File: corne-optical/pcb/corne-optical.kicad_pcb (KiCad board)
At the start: 2 copper layers, 145.7 x 94.9 mm, 77 parts, among them J1 MJ-4PP-9, J2 OLED, J3 LED, J4 Conn_01x02, J5 Conn_01x02, P1 i2c-pin, P2 i2c-pin, SW1 SW_PUSH, SW10 SW_PUSH, SW11 SW_PUSH, SW12 SW_PUSH, SW13 SW_PUSH, SW14 SW_PUSH, SW15 SW_PUSH, SW16 SW_PUSH, SW17 SW_PUSH, SW18 SW_PUSH, SW19 SW_PUSH, SW2 SW_PUSH, SW20 SW_PUSH, SW21 SW_PUSH, SW3 SW_PUSH, SW4 SW_PUSH, SW5 SW_PUSH, SW6 SW_PUSH, SW7 SW_PUSH, SW8 SW_PUSH, SW9 SW_PUSH, U1 ProMicro

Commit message: Trying to workout phantom copper
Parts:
- removed ? (x7): , kbd:LEGO_HOLE
- removed D1, D10, D11, D12, D13, D14, D15, D16, D17, D18, D19, D2, D20, D21, D3, D4, D5, D6, D7, D8, D9: D, kbd:D3_SMD
- removed G*** (x2): LOGO, kbd:corne
- removed L22, L23, L24, L25, L26, L27: SK6812MINI, kbd:SK6812MINI_underglow_rev
- added Q1: Q_NMOS_GSD, Package_TO_SOT_SMD:SOT-23, F.Cu at (75.7, 106.0)
- added Q2: Q_NMOS_GSD, Package_TO_SOT_SMD:SOT-23, F.Cu at (96.0, 106.0)
- added Q3: Q_NMOS_GSD, Package_TO_SOT_SMD:SOT-23, F.Cu at (113.7, 100.8)
- added Q4: Q_NMOS_GSD, Package_TO_SOT_SMD:SOT-23, F.Cu at (132.8, 98.5)
- added Q5: Q_NMOS_GSD, Package_TO_SOT_SMD:SOT-23, F.Cu at (153.5, 100.9)
- added Q6: Q_NMOS_GSD, Package_TO_SOT_SMD:SOT-23, F.Cu at (169.2, 103.2)
- added R10: 70R, Resistor_SMD:R_0603_1608Metric, F.Cu at (61.8, 80.8)
- added R11: 70R, Resistor_SMD:R_0603_1608Metric, F.Cu at (81.0, 80.3)
- added R3: 70R, Resistor_SMD:R_0603_1608Metric, F.Cu at (100.0, 76.3)
- added R4: 70R, Resistor_SMD:R_0603_1608Metric, F.Cu at (118.7, 73.9)
- added R5: 70R, Resistor_SMD:R_0603_1608Metric, F.Cu at (138.2, 76.2)
- added R6: 70R, Resistor_SMD:R_0603_1608Metric, F.Cu at (157.0, 78.6)
- added R7: 190R, Resistor_SMD:R_0603_1608Metric, F.Cu at (145.0, 122.5)
- added R8: 190R, Resistor_SMD:R_0603_1608Metric, F.Cu at (167.6, 130.1)
- added R9: 190R, Resistor_SMD:R_0603_1608Metric, F.Cu at (173.9, 128.3)
- J2: value OLED -> Conn_01x04
- J3: value LED -> Conn_01x03
- JP1: value (none) -> SolderJumper_2_Bridged
- JP2, JP3, JP4, JP5, JP6, JP7, JP8, JP9: value (none) -> SolderJumper_2_Open
- P1, P2: value i2c-pin -> Conn_01x01
- RSW1: value SW_PUSH -> SW_Push
- SW1, SW10, SW11, SW12, SW13, SW14, SW15, SW16, SW17, SW18, SW19, SW2, SW20, SW3, SW4, SW5, SW6, SW7, SW8, SW9: value SW_PUSH -> Keychron_LP_Optical; footprint kbd:Choc_Hotswap -> optical:Keychron_LP_Optical
- SW21: value SW_PUSH -> Keychron_LP_Optical; footprint kbd:Choc_Hotswap_1.5u -> optical:Keychron_LP_Optical_1.5u
- turned SW1 to 0 degrees
- turned SW10 to 0 degrees
- turned SW11 to 0 degrees
- turned SW12 to 0 degrees
- turned SW13 to 0 degrees
- turned SW14 to 0 degrees
- turned SW15 to 0 degrees
- turned SW16 to 0 degrees
- turned SW17 to 0 degrees
- turned SW18 to 0 degrees
- turned SW19 to 0 degrees
- turned SW2 to 0 degrees
- turned SW20 to -15 degrees
- turned SW21 to -30 degrees
- turned SW3 to 0 degrees
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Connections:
- SW1 pad 1: col0 -> Net-(R10-Pad2)
- SW1 pad 2: Net-(D1-Pad2) -> Net-(SW1-Pad2)
- SW10 pad 1: col3 -> Net-(SW10-Pad1)
- SW10 pad 2: Net-(D10-Pad2) -> Net-(SW10-Pad2)
- SW11 pad 1: col4 -> Net-(SW11-Pad1)
- SW11 pad 2: Net-(D11-Pad2) -> Net-(SW11-Pad2)
- SW12 pad 1: col5 -> Net-(SW12-Pad1)
- SW12 pad 2: Net-(D12-Pad2) -> Net-(SW12-Pad2)
- SW13 pad 1: col0 -> Net-(SW13-Pad1)
- SW13 pad 2: Net-(D13-Pad2) -> /col0_sink
- SW14 pad 1: col1 -> Net-(SW14-Pad1)
- SW14 pad 2: Net-(D14-Pad2) -> /col1_sink
- SW15 pad 1: col2 -> Net-(SW15-Pad1)
- SW15 pad 2: Net-(D15-Pad2) -> unconnected-(SW15-Pad2)
- SW16 pad 1: col3 -> Net-(SW10-Pad2)
- SW16 pad 2: Net-(D16-Pad2) -> /col3_sink
- SW17 pad 1: col4 -> Net-(SW11-Pad2)
- SW17 pad 2: Net-(D17-Pad2) -> /col4_sink
- SW18 pad 1: col5 -> Net-(SW12-Pad2)
- SW18 pad 2: Net-(D18-Pad2) -> /col5_sink
- SW19 pad 1: col3 -> Net-(R7-Pad2)
- SW19 pad 2: Net-(D19-Pad2) -> /col3_sink
- SW2 pad 1: col1 -> Net-(R11-Pad2)
- SW2 pad 2: Net-(D2-Pad2) -> Net-(SW2-Pad2)
- SW20 pad 1: col4 -> Net-(R8-Pad2)
- SW20 pad 2: Net-(D20-Pad2) -> /col4_sink
- SW21 pad 1: col5 -> Net-(R9-Pad2)
- SW21 pad 2: Net-(D21-Pad2) -> /col5_sink
- SW3 pad 1: col2 -> Net-(R3-Pad2)
- SW3 pad 2: Net-(D3-Pad2) -> Net-(SW3-Pad2)
- SW4 pad 1: col3 -> Net-(R4-Pad2)
- SW4 pad 2: Net-(D4-Pad2) -> Net-(SW10-Pad1)
- SW5 pad 1: col4 -> Net-(R5-Pad2)
- SW5 pad 2: Net-(D5-Pad2) -> Net-(SW11-Pad1)
- SW6 pad 1: col5 -> Net-(R6-Pad2)
- SW6 pad 2: Net-(D6-Pad2) -> Net-(SW12-Pad1)
- SW7 pad 1: col0 -> Net-(SW1-Pad2)
- SW7 pad 2: Net-(D7-Pad2) -> Net-(SW13-Pad1)
- SW8 pad 1: col1 -> Net-(SW2-Pad2)
- SW8 pad 2: Net-(D8-Pad2) -> Net-(SW14-Pad1)
- SW9 pad 1: col2 -> Net-(SW3-Pad2)
- SW9 pad 2: Net-(D9-Pad2) -> Net-(SW15-Pad1)
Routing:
- net GND: track 412.9 -> 0.00 mm, vias 13 -> 0
- net col0: track 239.4 -> 14.7 mm, vias 6 -> 2
- net col1: track 220.3 -> 0.00 mm, vias 6 -> 0
- net VCC: track 389.0 -> 176.6 mm, vias 12 -> 11
- net col3: track 214.9 -> 15.6 mm, vias 8 -> 2
- net col2: track 188.6 -> 0.00 mm, vias 6 -> 0
- net col4: track 184.7 -> 0.00 mm, vias 8 -> 0
- net col5: track 191.4 -> 15.9 mm, vias 7 -> 2
- net row2: track 178.7 -> 17.1 mm, vias 8 -> 0
- net row1: track 155.8 -> 0.00 mm, vias 8 -> 0
- net row0: track 168.8 -> 22.4 mm, vias 10 -> 1
- net row3: track 102.8 -> 17.1 mm, vias 3 -> 0
- net Net-(L25-Pad1): track 58.9 -> 0.00 mm, vias 5 -> 0
- net Net-(L23-Pad3): track 50.0 -> 0.00 mm, vias 4 -> 0
- net Net-(D21-Pad2): track 49.9 -> 0.00 mm, vias 2 -> 0
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
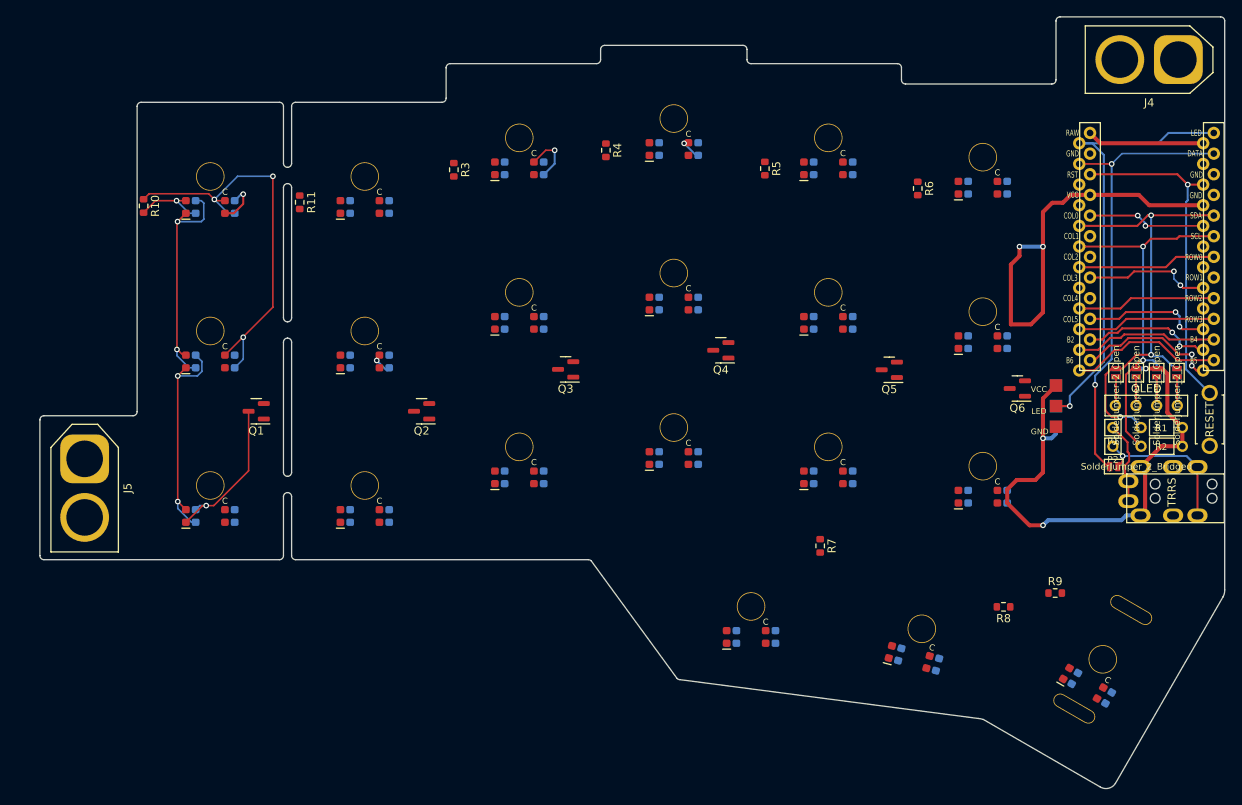
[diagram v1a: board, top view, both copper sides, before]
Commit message: Fixed outline, just trying to solve switch footprint glitch
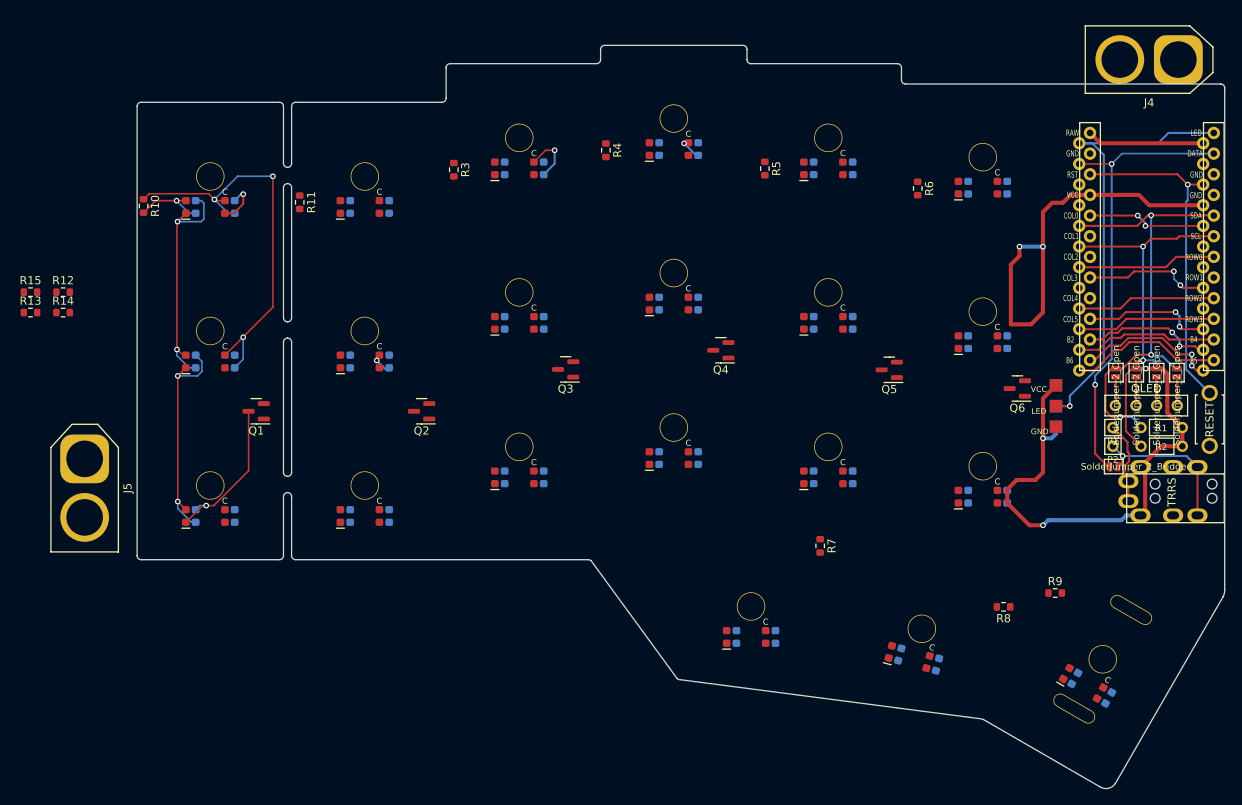
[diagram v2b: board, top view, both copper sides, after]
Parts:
- added R12: 1k, Resistor_SMD:R_0603_1608Metric, F.Cu at (51.9, 91.3)
- added R13: 1k, Resistor_SMD:R_0603_1608Metric, F.Cu at (47.9, 93.9)
- added R14: 1k, Resistor_SMD:R_0603_1608Metric, F.Cu at (51.9, 93.9)
- added R15: 1k, Resistor_SMD:R_0603_1608Metric, F.Cu at (47.9, 91.3)
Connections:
- SW1 pad 3: VCC -> row0
- SW1 pad 4: row0 -> GND
- SW10 pad 3: VCC -> row1
- SW10 pad 4: row1 -> GND
- SW11 pad 3: VCC -> row1
- SW11 pad 4: row1 -> GND
- SW12 pad 3: VCC -> row1
- SW12 pad 4: row1 -> GND
- SW13 pad 3: VCC -> row2
- SW13 pad 4: row2 -> GND
- SW14 pad 3: VCC -> row2
- SW14 pad 4: row2 -> GND
- SW15 pad 2: unconnected-(SW15-Pad2) -> /col2_sink
- SW15 pad 3: VCC -> row2
- SW15 pad 4: row2 -> GND
- SW16 pad 3: VCC -> row2
- SW16 pad 4: row2 -> GND
- SW17 pad 3: VCC -> row2
- SW17 pad 4: row2 -> GND
- SW18 pad 3: VCC -> row2
- SW18 pad 4: row2 -> GND
- SW19 pad 3: VCC -> row3
- SW19 pad 4: row3 -> GND
- SW2 pad 3: VCC -> row0
- SW2 pad 4: row0 -> GND
- SW20 pad 3: VCC -> row3
- SW20 pad 4: row3 -> GND
- SW21 pad 3: VCC -> row3
- SW21 pad 4: row3 -> GND
- SW3 pad 3: VCC -> row0
- SW3 pad 4: unconnected-(SW3-Pad4) -> GND
- SW4 pad 3: VCC -> row0
- SW4 pad 4: row0 -> GND
- SW5 pad 3: VCC -> row0
- SW5 pad 4: row0 -> GND
- SW6 pad 3: VCC -> row0
- SW6 pad 4: row0 -> GND
- SW7 pad 3: VCC -> row1
- SW7 pad 4: row1 -> GND
- SW8 pad 3: VCC -> row1
- SW8 pad 4: row1 -> GND
- SW9 pad 3: VCC -> row1
- SW9 pad 4: row1 -> GND
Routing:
- net VCC: track 176.6 -> 115.2 mm, vias 11 -> 5
- net row0: track 22.4 -> 76.7 mm, vias 1 -> 5
- net GND: track 0.00 -> 5.31 mm, vias 0 -> 1
- net row1: track 0.00 -> 1.77 mm, vias 0 -> 1
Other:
- board size 145.7 x 94.9 mm -> 133.8 x 91.4 mm

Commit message: Finished, but need to add mounting holes for plate
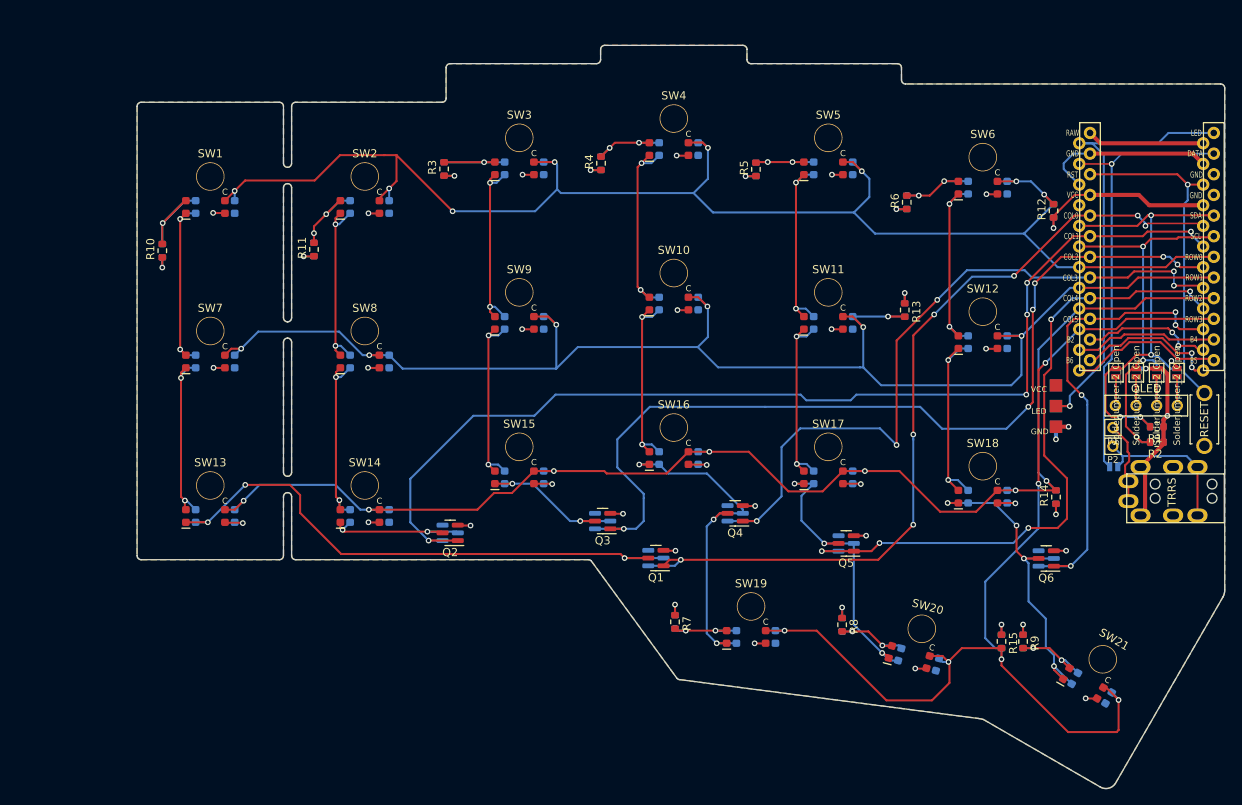
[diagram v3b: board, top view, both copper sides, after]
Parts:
- removed J4, J5: Conn_01x02, Connector_AMASS:AMASS_XT60-F_1x02_P7.20mm_Vertical
- JP1: moved to B.Cu
- R1, R2: footprint kbd:R -> optical:R_0603_1608Metric
- R10, R11, R12, R13, R14, R15, R3, R4, R5, R6, R7, R8, R9: footprint Resistor_SMD:R_0603_1608Metric -> optical:R_0603_1608Metric
- moved R15 126.9 mm to (167.3, 134.3), turned to -90 degrees
- moved R14 124.2 mm to (174.0, 116.5), turned to 90 degrees
- moved R12 122.2 mm to (173.7, 81.3), turned to 90 degrees
- moved R13 107.5 mm to (155.4, 93.5), turned to -90 degrees
- moved Q1 52.4 mm to (124.8, 124.0)
- moved Q5 22.0 mm to (148.2, 122.2)
- moved Q6 21.2 mm to (172.8, 124.1)
- moved R7 20.2 mm to (127.2, 131.9)
- moved Q4 20.1 mm to (134.6, 118.5)
- moved R8 20.0 mm to (147.7, 132.2), turned to -90 degrees
- moved Q3 19.2 mm to (118.2, 119.5)
- moved Q2 15.4 mm to (99.5, 121.0)
- moved R9 7.14 mm to (169.9, 134.3), turned to -90 degrees
- moved R11 6.06 mm to (82.8, 86.1), turned to 90 degrees
- moved R10 5.96 mm to (64.1, 86.2), turned to 90 degrees
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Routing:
- net row1: track 1.77 -> 183.6 mm, vias 1 -> 7
- net row2: track 17.1 -> 167.4 mm, vias 0 -> 7
- net col1: track 0.00 -> 133.5 mm, vias 0 -> 5
- net row3: track 17.1 -> 133.2 mm, vias 0 -> 6
- net col2: track 0.00 -> 112.0 mm, vias 0 -> 6
- net row0: track 76.7 -> 186.0 mm, vias 5 -> 8
- net col0: track 14.7 -> 103.2 mm, vias 2 -> 7
- net col4: track 0.00 -> 81.2 mm, vias 0 -> 5
- net col3: track 15.6 -> 88.3 mm, vias 2 -> 5
- net GND: track 5.31 -> 67.0 mm, vias 1 -> 29
- net /col0_sink: track 19.2 -> 70.1 mm, vias 1 -> 3
- net /col3_sink: track 0.00 -> 42.4 mm, vias 0 -> 3
- net col5: track 15.9 -> 56.7 mm, vias 2 -> 4
- net /col5_sink: track 0.00 -> 40.8 mm, vias 0 -> 4
- net /col4_sink: track 0.00 -> 36.4 mm, vias 0 -> 3
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- added copper zone on B.Cu, net GND
- added copper zone on F.Cu, net VCC
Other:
- rule pad_to_mask_clearance: 0.2 -> 0

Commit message: Holes done and board sent off
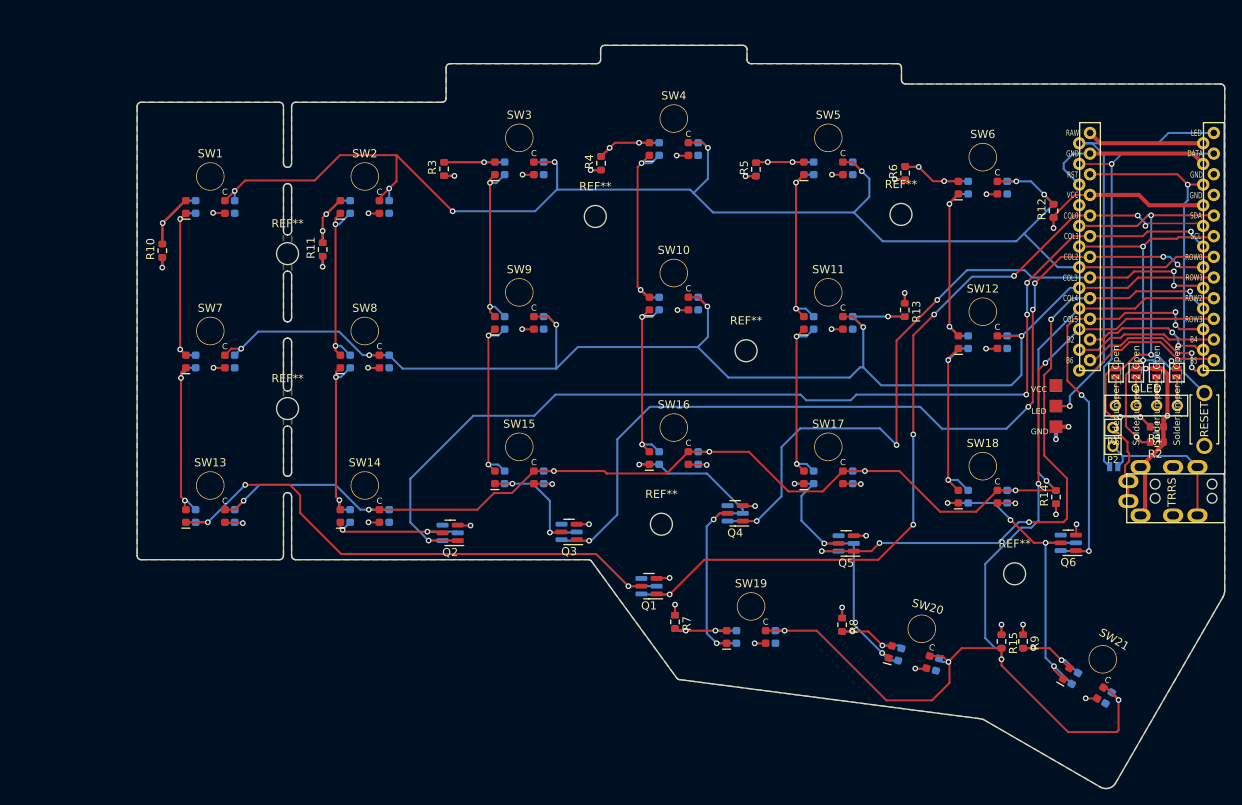
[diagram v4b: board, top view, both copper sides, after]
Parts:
- added REF**: MountingHole_2.7mm_M2.5, MountingHole:MountingHole_2.7mm_M2.5, F.Cu at (79.5, 86.6)
- added REF**: MountingHole_2.7mm_M2.5, MountingHole:MountingHole_2.7mm_M2.5, F.Cu at (135.9, 98.6)
- added REF**: MountingHole_2.7mm_M2.5, MountingHole:MountingHole_2.7mm_M2.5, F.Cu at (154.9, 81.8)
- added REF**: MountingHole_2.7mm_M2.5, MountingHole:MountingHole_2.7mm_M2.5, F.Cu at (117.3, 82.0)
- added REF**: MountingHole_2.7mm_M2.5, MountingHole:MountingHole_2.7mm_M2.5, F.Cu at (125.5, 119.9)
- added REF**: MountingHole_2.7mm_M2.5, MountingHole:MountingHole_2.7mm_M2.5, F.Cu at (79.5, 105.7)
- added REF**: MountingHole_2.7mm_M2.5, MountingHole:MountingHole_2.7mm_M2.5, F.Cu at (168.9, 126.0)
- moved Q3 4.34 mm to (114.1, 120.8)
- moved R6 3.60 mm to (155.4, 76.7)
- moved Q1 3.56 mm to (124.0, 127.5)
- moved Q6 3.33 mm to (175.5, 122.2)
- moved R11 1.07 mm to (83.8, 86.1)
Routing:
- net col5: track 56.7 -> 53.0 mm
- net /col2_sink: track 18.9 -> 17.3 mm
- net col0: track 103.2 -> 104.7 mm
- net row1: track 183.6 -> 184.7 mm
- net /col5_sink: track 40.8 -> 41.8 mm
- net row0: track 186.0 -> 186.8 mm
- net /col0_sink: track 70.1 -> 69.3 mm
- net row3: track 133.2 -> 133.9 mm
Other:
- outline, holes or cut-outs redrawn
